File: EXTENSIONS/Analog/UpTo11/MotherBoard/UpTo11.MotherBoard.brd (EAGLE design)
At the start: 48 x 38 mm, 9 parts, among them X1 USB-A

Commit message: Create UpTo11
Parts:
- moved CAP_100UF 7.07 mm to (28.0, 31.0)
- moved R_100_O 5.00 mm to (17.0, 27.0)
- moved R_22_O 4.00 mm to (38.0, 27.0)
- moved 2N3904_NPN 1.41 mm to (41.7, 37.0)
- moved 2N3906_PNP 1.41 mm to (13.2, 37.0)
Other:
- board text added: "GND"
- board text added: "LED_FLASH"
- board text added: "LED_PWR"
- board text added: "POT_IN"
- board text added: "POT_OUT"
- board text added: "Up To 11 - Mother Board"
- board text added: "VCC"
- board text added: "bit.ly/38Kq3UG"
- board text added: "https://bit.ly/38Kq3UG"
- board text added: "www.FredericTorres.com"
- board text removed: "1 LED"
- board text removed: "Blinker"
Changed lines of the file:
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@@
 <layer number="23" name="tOrigins" color="15" fill="1" visible="yes" active="yes"/>
 <layer number="24" name="bOrigins" color="15" fill="1" visible="yes" active="yes"/>
-<layer number="25" name="tNames" color="7" fill="1" visible="no" active="yes"/>
-<layer number="26" name="bNames" color="7" fill="1" visible="yes" active="yes"/>
+<layer number="25" name="tNames" color="7" fill="1" visible="yes" active="yes"/>
+<layer number="26" name="bNames" color="7" fill="1" visible="no" active="yes"/>
 <layer number="27" name="tValues" color="7" fill="1" visible="yes" active="yes"/>
 <layer number="28" name="bValues" color="7" fill="1" visible="yes" active="yes"/>
@@
 <wire x1="50" y1="50" x2="2" y2="50" width="0" layer="20"/>
 <wire x1="2" y1="50" x2="2" y2="12" width="0" layer="20"/>
-<text x="7.5" y="53" size="1.016" layer="25" rot="R180">1 LED</text>
-<text x="20" y="53" size="1.016" layer="25" rot="R180">Blinker</text>
+<text x="4.5" y="31" size="1.4224" layer="25" rot="R270" align="center">Up To 11 - Mother Board</text>
 <text x="26.5" y="27" size="2.1844" layer="26" rot="MR0" align="center">MadeInTheUSB.net</text>
 <text x="3.5" y="31" size="1.27" layer="26" rot="MR90" align="center">PCBv1 - 2019.12</text>
-<text x="27.5" y="43" size="2.1844" layer="26" rot="MR0" align="center">Up To 11 - MotherBoard</text>
+<text x="26" y="45" size="2.1844" layer="26" rot="MR0" align="center">Up To 11 - MotherBoard</text>
+<text x="48.5" y="27" size="1.4224" layer="26" rot="MR270" align="center">www.FredericTorres.com</text>
+<text x="25" y="42" size="1.6764" layer="26" rot="MR0" align="center">https://bit.ly/38Kq3UG</text>
+<text x="41.5" y="16" size="1.016" layer="25" align="center">bit.ly/38Kq3UG</text>
+<text x="19.5" y="45" size="1.016" layer="25" rot="R90" align="center">GND</text>
+<text x="22.5" y="45" size="1.016" layer="25" rot="R90" align="center">VCC</text>
+<text x="25" y="43" size="1.016" layer="25" rot="R90" align="center">LED_PWR</text>
+<text x="27.5" y="42" size="1.016" layer="25" rot="R90" align="center">LED_FLASH</text>
+<text x="30" y="44" size="1.016" layer="25" rot="R90" align="center">POT_IN</text>
+<text x="32.5" y="43" size="1.016" layer="25" rot="R90" align="center">POT_OUT</text>
 </plain>
 <attributes>
@@
 </autorouter>
 <elements>
-<element name="CAP_100UF" library="adafruit" package="C025-030X050" value="" x="27" y="38" smashed="yes">
-<attribute name="NAME" x="24" y="34.905" size="0.8128" layer="25" ratio="10"/>
-<attribute name="VALUE" x="24.714" y="34.952" size="1.27" layer="27" ratio="10"/>
-</element>
-<element name="R_100_O" library="adafruit" package="0207/10" value="" x="22" y="27" smashed="yes" rot="R90">
-<attribute name="NAME" x="19.476" y="26.952" size="1.27" layer="25" ratio="10" rot="R90" align="center"/>
-<attribute name="VALUE" x="22.635" y="24.7394" size="1.27" layer="27" ratio="10" rot="R90"/>
-</element>
-<element name="R_22_O" library="adafruit" package="0207/10" value="" x="34" y="27" smashed="yes" rot="R270">
-<attribute name="NAME" x="31.524" y="27.048" size="1.27" layer="25" ratio="10" rot="R270" align="center"/>
-<attribute name="VALUE" x="33.365" y="29.2606" size="1.27" layer="27" ratio="10" rot="R270"/>
+<element name="CAP_100UF" library="adafruit" package="C025-030X050" value="" x="28" y="31" smashed="yes">
+<attribute name="NAME" x="25" y="27.905" size="0.8128" layer="25" ratio="10"/>
+<attribute name="VALUE" x="25.714" y="27.952" size="1.27" layer="27" ratio="10"/>
+</element>
+<element name="R_100_O" library="adafruit" package="0207/10" value="" x="17" y="27" smashed="yes" rot="R90">
+<attribute name="NAME" x="19.476" y="26.952" size="1.016" layer="25" ratio="10" rot="R90" align="center"/>
+<attribute name="VALUE" x="17.635" y="24.7394" size="1.27" layer="27" ratio="10" rot="R90"/>
+</element>
+<element name="R_22_O" library="adafruit" package="0207/10" value="" x="38" y="27" smashed="yes" rot="R270">
+<attribute name="NAME" x="40.524" y="27.048" size="1.016" layer="25" ratio="10" rot="R270" align="center"/>
+<attribute name="VALUE" x="37.365" y="29.2606" size="1.27" layer="27" ratio="10" rot="R270"/>
 </element>
 <element name="R_1M_O" library="adafruit" package="0207/10" value="" x="8" y="27" smashed="yes" rot="R90">
-<attribute name="NAME" x="5.476" y="26.952" size="1.27" layer="25" ratio="10" rot="R90" align="center"/>
+<attribute name="NAME" x="10.476" y="26.952" size="1.016" layer="25" ratio="10" rot="R90" align="center"/>
 <attribute name="VALUE" x="8.635" y="24.7394" size="1.27" layer="27" ratio="10" rot="R90"/>
 </element>
-<element name="2N3904_NPN" library="transistor" package="TO92" value="2N3904" x="40.7" y="38" smashed="yes" rot="R270">
-<attribute name="NAME" x="40.3" y="42" size="1.27" layer="25" ratio="10" align="center"/>
-</element>
-<element name="2N3906_PNP" library="transistor-pnp" package="TO92" value="2N3906" x="14.2" y="38" smashed="yes" rot="R90">
-<attribute name="NAME" x="14.5" y="42" size="1.27" layer="25" ratio="10" align="center"/>
+<element name="2N3904_NPN" library="transistor" package="TO92" value="2N3904" x="41.7" y="37" smashed="yes" rot="R270">
+<attribute name="NAME" x="41.3" y="41" size="1.016" layer="25" ratio="10" align="center"/>
+</element>
+<element name="2N3906_PNP" library="transistor-pnp" package="TO92" value="2N3906" x="13.2" y="37" smashed="yes" rot="R90">
+<attribute name="NAME" x="13.5" y="41" size="1.016" layer="25" ratio="10" align="center"/>
 </element>
 <element name="X1" library="adafruit" package="MOLEX_480371000" value="USB-A" x="25" y="16" smashed="yes">
@@
 </element>
 <element name="FRONT_PANEL_INTERFACE" library="adafruit" package="1X06" value="" x="26" y="48" smashed="yes">
-<attribute name="NAME" x="26.3038" y="44.8288" size="1.27" layer="25" ratio="10" align="center"/>
+<attribute name="NAME" x="9.8038" y="47.8288" size="0.8128" layer="25" ratio="10" align="center"/>
 <attribute name="VALUE" x="18.38" y="44.825" size="1.27" layer="27"/>
 </element>
 <element name="R_PWR_LED_1K" library="adafruit" package="0207/10" value="" x="46" y="27" smashed="yes" rot="R270">
-<attribute name="NAME" x="48.524" y="27.048" size="1.27" layer="25" ratio="10" rot="R270" align="center"/>
+<attribute name="NAME" x="48.524" y="27.048" size="1.016" layer="25" ratio="10" rot="R270" align="center"/>
 <attribute name="VALUE" x="45.365" y="29.2606" size="1.27" layer="27" ratio="10" rot="R270"/>
 </element>
@@
 <contactref element="2N3904_NPN" pad="1"/>
 <contactref element="CAP_100UF" pad="2"/>
-<wire x1="34" y1="32.08" x2="40.7" y2="36.73" width="0" layer="19" extent="1-1"/>
-<wire x1="28.27" y1="38" x2="34" y2="32.08" width="0" layer="19" extent="1-1"/>
+<wire x1="38" y1="32.08" x2="41.7" y2="35.73" width="0" layer="19" extent="1-1"/>
+<wire x1="29.27" y1="31" x2="38" y2="32.08" width="0" layer="19" extent="1-1"/>
 </signal>
 <signal name="LED_FLASH">
 <contactref element="2N3904_NPN" pad="3"/>
 <contactref element="FRONT_PANEL_INTERFACE" pad="4"/>
-<wire x1="27.27" y1="48" x2="40.7" y2="39.27" width="0" layer="19" extent="1-1"/>
+<wire x1="27.27" y1="48" x2="41.7" y2="38.27" width="0" layer="19" extent="1-1"/>
 </signal>
 <signal name="GND_EX">
@@
 <contactref element="2N3906_PNP" pad="2"/>
 <contactref element="R_1M_O" pad="2"/>
-<wire x1="12.295" y1="38" x2="25.73" y2="38" width="0" layer="19" extent="1-1"/>
-<wire x1="8" y1="32.08" x2="12.295" y2="38" width="0" layer="19" extent="1-1"/>
+<wire x1="11.295" y1="37" x2="26.73" y2="31" width="0" layer="19" extent="1-1"/>
+<wire x1="8" y1="32.08" x2="11.295" y2="37" width="0" layer="19" extent="1-1"/>
 </signal>
 <signal name="N$6">
 <contactref element="2N3906_PNP" pad="1"/>
 <contactref element="R_100_O" pad="1"/>
-<wire x1="22" y1="21.92" x2="14.2" y2="39.27" width="0" layer="19" extent="1-1"/>
+<wire x1="17" y1="21.92" x2="13.2" y2="38.27" width="0" layer="19" extent="1-1"/>
 </signal>
 <signal name="VCC">
@@
 <contactref element="2N3906_PNP" pad="3"/>
 <contactref element="R_PWR_LED_1K" pad="2"/>
-<wire x1="14.2" y1="36.73" x2="22.19" y2="48" width="0" layer="19" extent="1-1"/>
-<wire x1="28.5" y1="18.6" x2="14.2" y2="36.73" width="0" layer="19" extent="1-1"/>
-<wire x1="34" y1="21.92" x2="28.5" y2="18.6" width="0" layer="19" extent="1-1"/>
-<wire x1="46" y1="21.92" x2="34" y2="21.92" width="0" layer="19" extent="1-1"/>
+<wire x1="13.2" y1="35.73" x2="22.19" y2="48" width="0" layer="19" extent="1-1"/>
+<wire x1="28.5" y1="18.6" x2="13.2" y2="35.73" width="0" layer="19" extent="1-1"/>
+<wire x1="38" y1="21.92" x2="28.5" y2="18.6" width="0" layer="19" extent="1-1"/>
+<wire x1="46" y1="21.92" x2="38" y2="21.92" width="0" layer="19" extent="1-1"/>
 </signal>
 <signal name="LED_PWR">
@@
 <contactref element="R_100_O" pad="2"/>
 <contactref element="FRONT_PANEL_INTERFACE" pad="5"/>
-<wire x1="22" y1="32.08" x2="29.81" y2="48" width="0" layer="19" extent="1-1"/>
+<wire x1="17" y1="32.08" x2="29.81" y2="48" width="0" layer="19" extent="1-1"/>
 </signal>
 <signal name="POT_OUT">
 <contactref element="2N3904_NPN" pad="2"/>
 <contactref element="FRONT_PANEL_INTERFACE" pad="6"/>
-<wire x1="32.35" y1="48" x2="42.605" y2="38" width="0" layer="19" extent="1-1"/>
+<wire x1="32.35" y1="48" x2="43.605" y2="37" width="0" layer="19" extent="1-1"/>
 </signal>
 </signals>

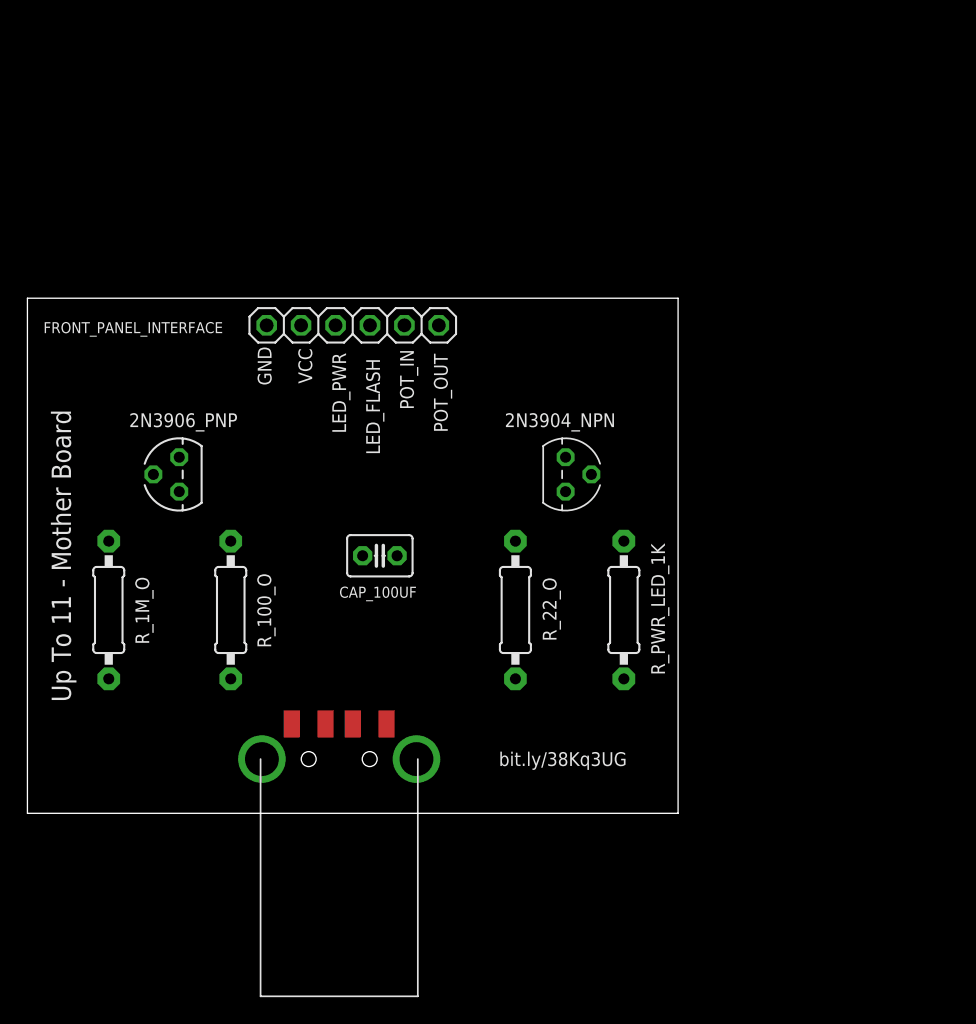
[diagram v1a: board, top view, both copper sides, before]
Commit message: Create UpTo11 Front Panel
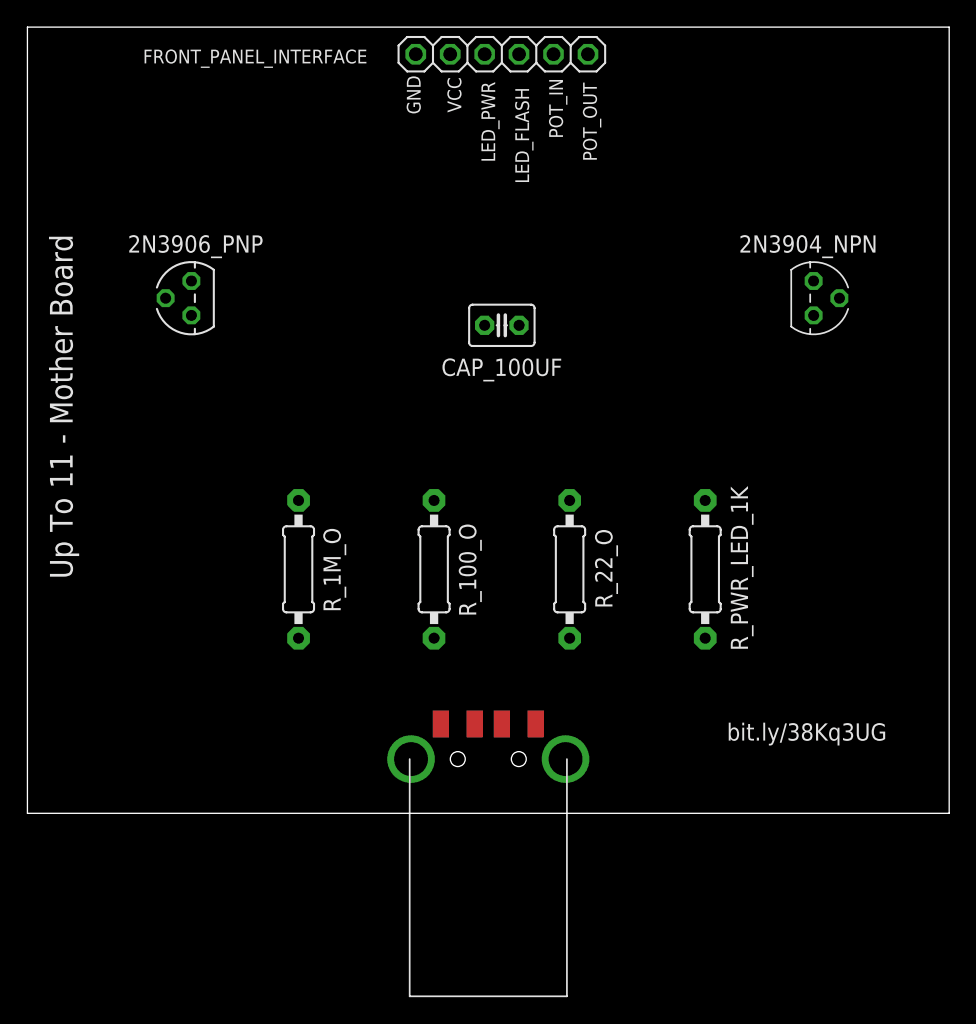
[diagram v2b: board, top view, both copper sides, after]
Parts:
- moved FRONT_PANEL_INTERFACE 22.8 mm to (37.0, 68.0)
- moved 2N3904_NPN 22.4 mm to (60.0, 50.0)
- moved CAP_100UF 19.2 mm to (37.0, 48.0)
- moved R_100_O 15.3 mm to (32.0, 30.0)
- moved R_1M_O 14.3 mm to (22.0, 30.0)
- moved 2N3906_PNP 13.0 mm to (14.1, 50.0)
- moved X1 11.0 mm to (36.0, 16.0)
- moved R_PWR_LED_1K 6.71 mm to (52.0, 30.0)
- moved R_22_O 5.00 mm to (42.0, 30.0)
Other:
- board size 48 x 38 mm -> 68 x 58 mm

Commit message: Create UpTo11 Front Panel
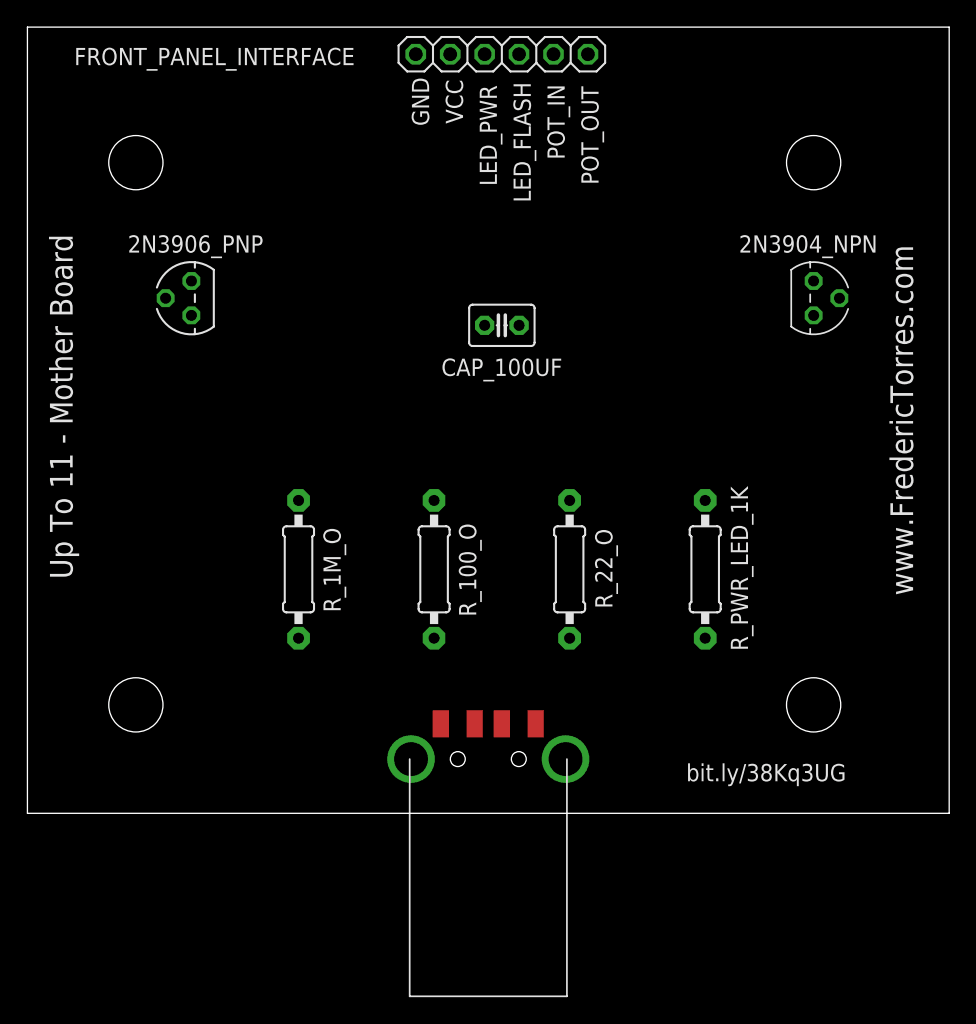
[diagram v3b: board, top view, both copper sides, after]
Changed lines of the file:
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@@
 <layer number="43" name="vRestrict" color="2" fill="10" visible="yes" active="yes"/>
 <layer number="44" name="Drills" color="7" fill="1" visible="no" active="yes"/>
-<layer number="45" name="Holes" color="7" fill="1" visible="no" active="yes"/>
+<layer number="45" name="Holes" color="7" fill="1" visible="yes" active="yes"/>
 <layer number="46" name="Milling" color="3" fill="1" visible="no" active="yes"/>
 <layer number="47" name="Measures" color="7" fill="1" visible="no" active="yes"/>
@@
 <text x="38.5" y="43" size="2.1844" layer="26" rot="MR0" align="center">MadeInTheUSB.net</text>
 <text x="4.5" y="21" size="1.27" layer="26" rot="MR90" align="center">PCBv1 - 2019.12</text>
-<text x="38" y="63" size="2.1844" layer="26" rot="MR0" align="center">Up To 11 - MotherBoard</text>
+<text x="36" y="63" size="2.1844" layer="26" rot="MR0" align="center">Up To 11 - MotherBoard</text>
 <text x="67.5" y="40" size="1.778" layer="26" rot="MR270" align="center">www.FredericTorres.com</text>
 <text x="36" y="56" size="1.6764" layer="26" rot="MR0" align="center">https://bit.ly/38Kq3UG</text>
-<text x="59.5" y="18" size="1.27" layer="25" align="center">bit.ly/38Kq3UG</text>
-<text x="30.5" y="65" size="1.016" layer="25" rot="R90" align="center">GND</text>
-<text x="33.5" y="65" size="1.016" layer="25" rot="R90" align="center">VCC</text>
-<text x="36" y="63" size="1.016" layer="25" rot="R90" align="center">LED_PWR</text>
-<text x="38.5" y="62" size="1.016" layer="25" rot="R90" align="center">LED_FLASH</text>
-<text x="41" y="64" size="1.016" layer="25" rot="R90" align="center">POT_IN</text>
-<text x="43.5" y="63" size="1.016" layer="25" rot="R90" align="center">POT_OUT</text>
+<text x="56.5" y="15" size="1.27" layer="25" align="center">bit.ly/38Kq3UG</text>
+<text x="31" y="64.5" size="1.27" layer="25" rot="R90" align="center">GND</text>
+<text x="33.5" y="64.5" size="1.27" layer="25" rot="R90" align="center">VCC</text>
+<text x="36" y="62" size="1.27" layer="25" rot="R90" align="center">LED_PWR</text>
+<text x="38.5" y="61.5" size="1.27" layer="25" rot="R90" align="center">LED_FLASH</text>
+<text x="41" y="63" size="1.27" layer="25" rot="R90" align="center">POT_IN</text>
+<text x="43.5" y="62" size="1.27" layer="25" rot="R90" align="center">POT_OUT</text>
+<hole x="10" y="60" drill="4"/>
+<hole x="10" y="20" drill="4"/>
+<hole x="60" y="60" drill="4"/>
+<hole x="60" y="20" drill="4"/>
+<text x="66.5" y="41" size="1.6764" layer="25" rot="R270" align="center">www.FredericTorres.com</text>
 </plain>
 <attributes>
@@
 </element>
 <element name="FRONT_PANEL_INTERFACE" library="adafruit" package="1X06" value="" x="37" y="68" smashed="yes">
-<attribute name="NAME" x="18.8038" y="67.8288" size="1.016" layer="25" ratio="10" align="center"/>
+<attribute name="NAME" x="15.8038" y="67.8288" size="1.27" layer="25" ratio="10" align="center"/>
 <attribute name="VALUE" x="29.38" y="64.825" size="1.27" layer="27"/>
 </element>
